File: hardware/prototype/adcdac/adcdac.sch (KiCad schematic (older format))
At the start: 68 parts, among them IC1 ADP3335, IC2 AD8138, IC3 AD8138, IC4 ADP3335, IC5 AD9744, IC6 ADP3335, IC7 ADP3335, IC8 AD8041, IC9 AD9218, J1 FPGA_GPIO0, J2 MODE, J3 S2, J4 S1, J5 DFS, P1 COAX, P2 COAX, P3 COAX

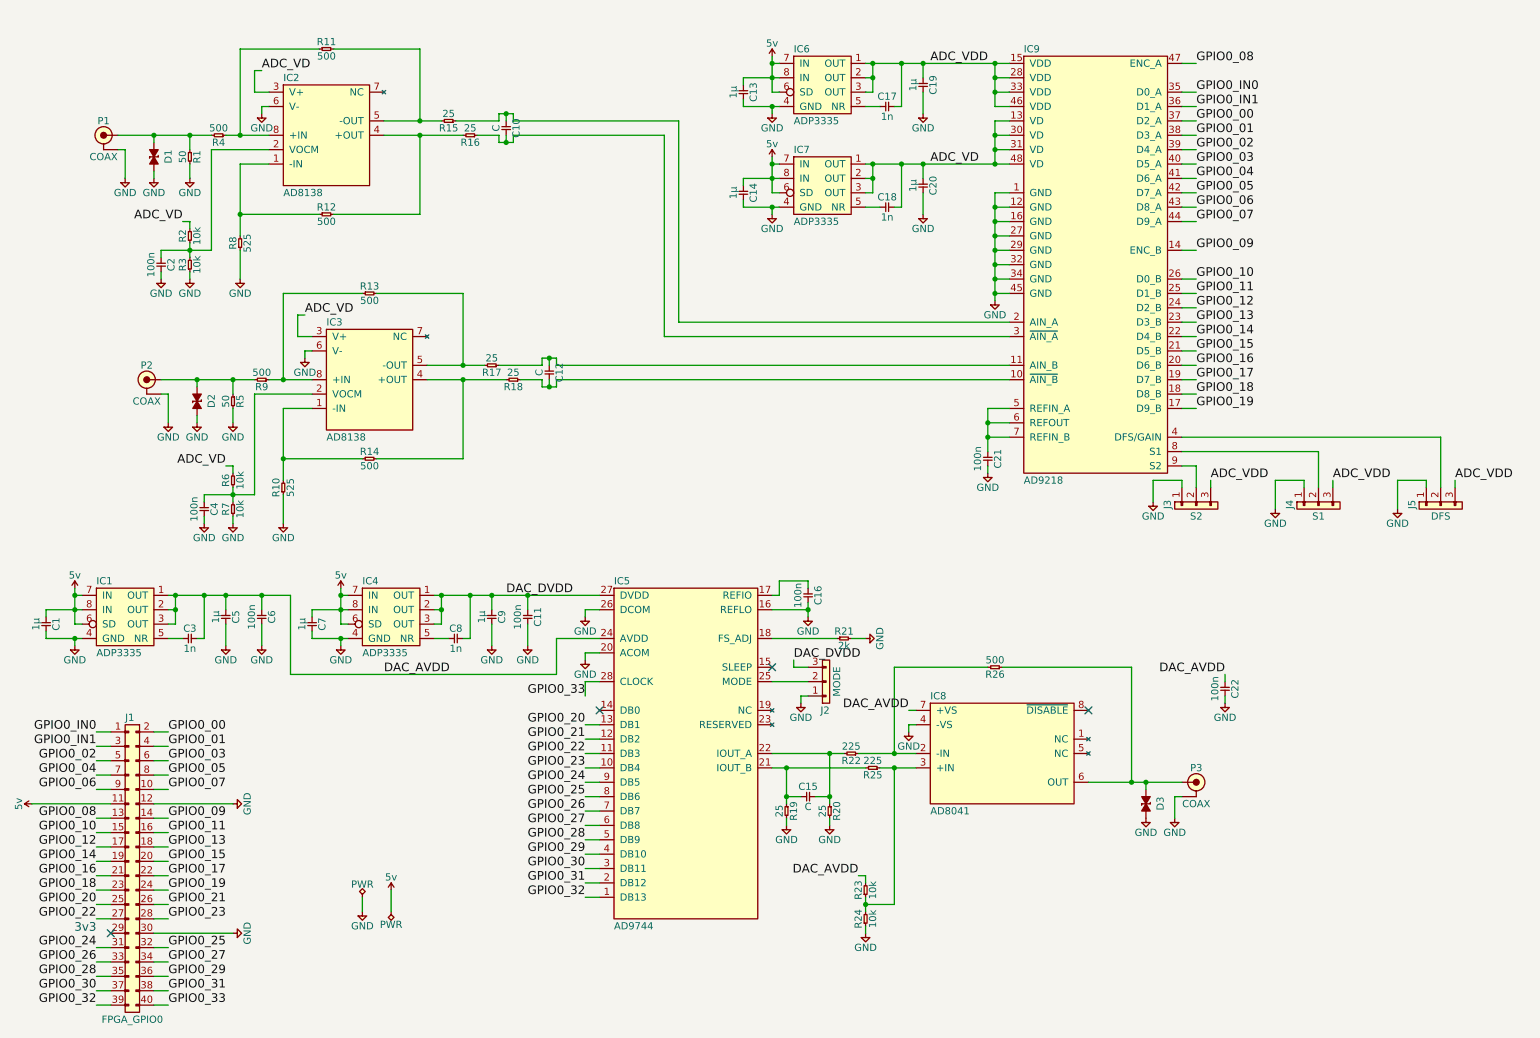
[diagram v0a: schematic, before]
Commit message: Minor sch tweaks
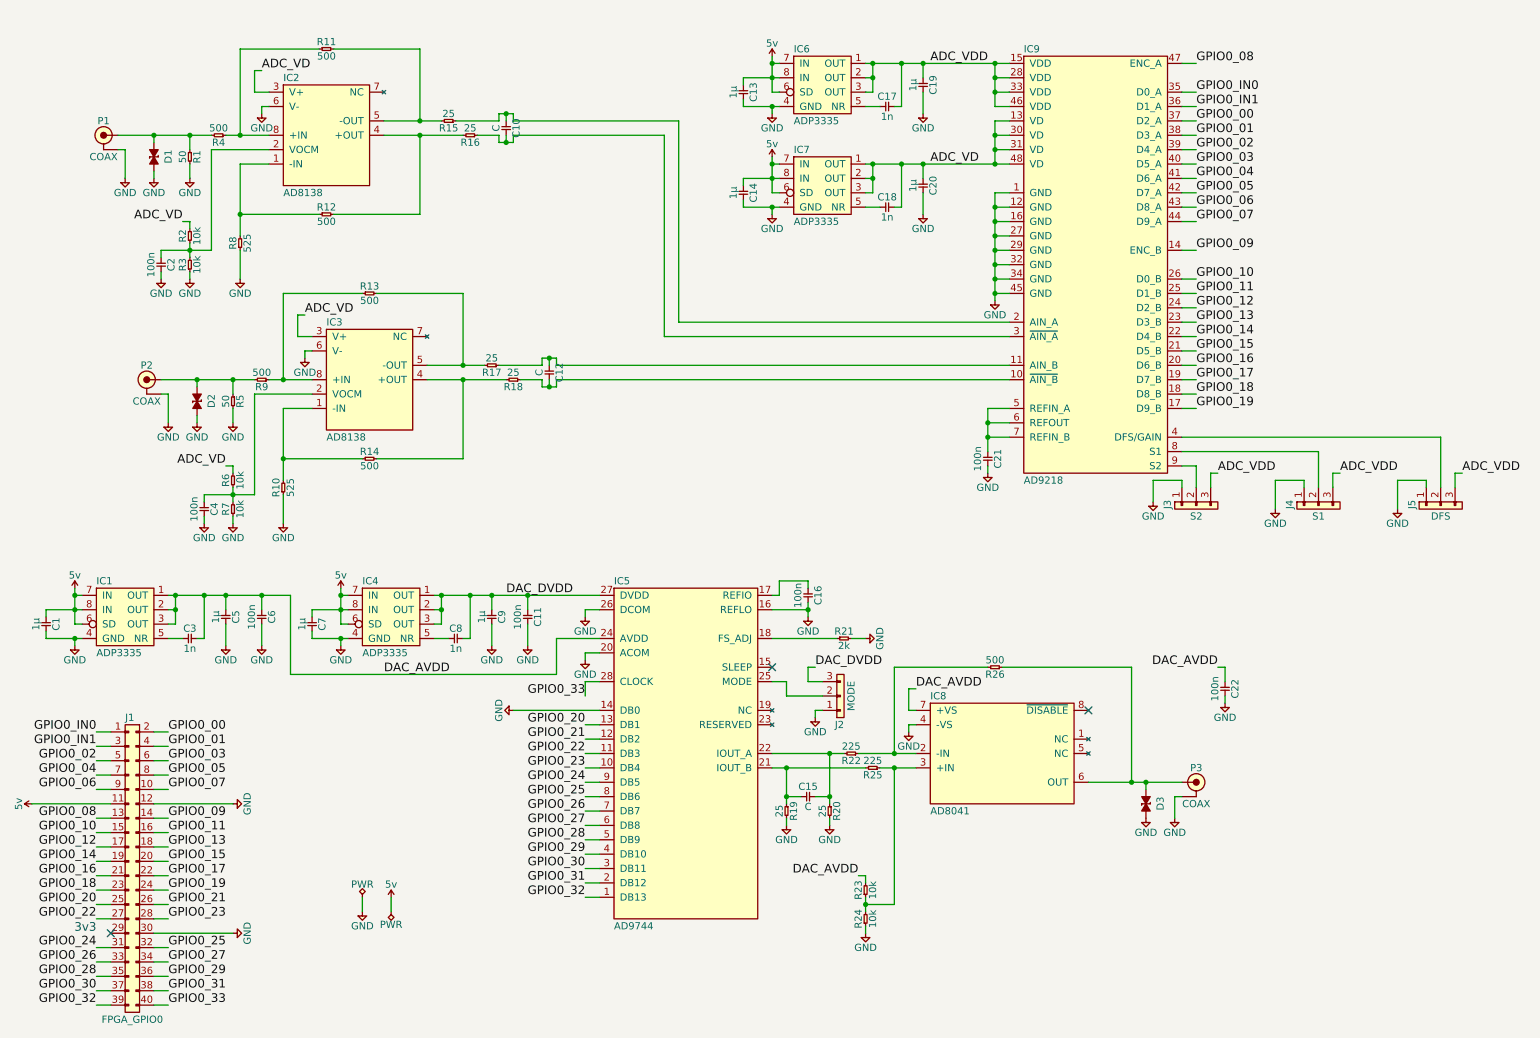
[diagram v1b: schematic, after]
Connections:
- net GND: now also IC5.14 (DB0)
- no-connect marks 4 -> 3
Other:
- moved on the sheet: J2
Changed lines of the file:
@@
 Text Label 8900 3350 0    60   ~ 0
 GPIO0_19
-NoConn ~ 4750 5450
 $Comp
 L 5v #PWR021
@@
 $EndComp
 NoConn ~ 8150 5450
-Text Label 6900 5450 2    60   ~ 0
+Text Label 6950 5300 0    60   ~ 0
 DAC_AVDD
 $Comp
@@
 Text Label 7050 1650 0    60   ~ 0
 ADC_VD
-Text Label 9100 5200 2    60   ~ 0
+Text Label 9050 5150 2    60   ~ 0
 DAC_AVDD
 $Comp
@@
 L CONN_01x03 J2
 U 1 1 59FA3731
-P 6300 5350
-F 0 "J2" H 6250 5450 50  0000 L CNN
-F 1 "MODE" V 6200 5250 50  0000 C CNN
-F 2 "agg:SIL-254P-03" H 6300 5350 50  0001 C CNN
-F 3 "" H 6300 5350 50  0001 C CNN
-	1    6300 5350
+P 6400 5450
+F 0 "J2" H 6350 5550 50  0000 L CNN
+F 1 "MODE" V 6300 5350 50  0000 C CNN
+F 2 "agg:SIL-254P-03" H 6400 5450 50  0001 C CNN
+F 3 "" H 6400 5450 50  0001 C CNN
+	1    6400 5450
 	-1   0    0    1
 $EndComp
@@
 L GND #PWR032
 U 1 1 59FA3B32
-P 6150 5400
-F 0 "#PWR032" H 6020 5440 50  0001 L CNN
-F 1 "GND" H 6150 5300 50  0000 C CNN
-F 2 "" H 6150 5400 60  0001 C CNN
-F 3 "" H 6150 5400 60  0001 C CNN
-	1    6150 5400
+P 6250 5500
+F 0 "#PWR032" H 6120 5540 50  0001 L CNN
+F 1 "GND" H 6250 5400 50  0000 C CNN
+F 2 "" H 6250 5500 60  0001 C CNN
+F 3 "" H 6250 5500 60  0001 C CNN
+	1    6250 5500
 	1    0    0    -1
 $EndComp
 Text Label 4100 4650 0    60   ~ 0
 DAC_DVDD
-Text Label 6100 5100 0    60   ~ 0
+Text Label 6250 5150 0    60   ~ 0
 DAC_DVDD
 $Comp
@@
 Text Label 7050 950  0    60   ~ 0
 ADC_VDD
-Text Label 9000 3850 0    60   ~ 0
+Text Label 9050 3800 0    60   ~ 0
 ADC_VDD
-Text Label 9850 3850 0    60   ~ 0
+Text Label 9900 3800 0    60   ~ 0
 ADC_VDD
-Text Label 10700 3850 0    60   ~ 0
+Text Label 10750 3800 0    60   ~ 0
 ADC_VDD
 $Comp
@@
 	9100 5400 9100 5350
 Wire Wire Line
-	9100 5200 9100 5250
+	9100 5150 9100 5250
 Wire Wire Line
 	5950 4750 6200 4750
@@
 	6400 4950 5950 4950
 Wire Wire Line
-	6200 5250 5950 5250
-Wire Wire Line
-	6200 5350 6150 5350
-Wire Wire Line
-	6150 5350 6150 5400
-Wire Wire Line
-	6100 5100 6100 5150
-Wire Wire Line
-	6100 5150 6200 5150
+	6300 5350 6050 5350
+Wire Wire Line
+	6300 5450 6250 5450
+Wire Wire Line
+	6250 5450 6250 5500
+Wire Wire Line
+	6200 5150 6200 5250
+Wire Wire Line
+	6200 5250 6300 5250
 Wire Wire Line
 	8800 3750 8900 3750
@@
 	10600 3550 10600 3900
 Wire Wire Line
-	9000 3850 9000 3900
-Wire Wire Line
-	9850 3850 9850 3900
-Wire Wire Line
-	10700 3850 10700 3900
+	9000 3800 9000 3900
+Wire Wire Line
+	9850 3800 9850 3900
+Wire Wire Line
+	10700 3800 10700 3900
 Wire Wire Line
 	8600 4000 8600 3850
@@
 L 5v #PWR048
 U 1 1 59FB00DD
-P 3300 6700
-F 0 "#PWR048" H 3300 6810 50  0001 L CNN
-F 1 "5v" H 3300 6790 50  0000 C CNN
-F 2 "" H 3300 6700 60  0001 C CNN
-F 3 "" H 3300 6700 60  0001 C CNN
-	1    3300 6700
+P 3300 6750
+F 0 "#PWR048" H 3300 6860 50  0001 L CNN
+F 1 "5v" H 3300 6840 50  0000 C CNN
+F 2 "" H 3300 6750 60  0001 C CNN
+F 3 "" H 3300 6750 60  0001 C CNN
+	1    3300 6750
 	1    0    0    -1
 $EndComp
@@
 $EndComp
 Wire Wire Line
-	3300 6850 3300 6700
+	3300 6850 3300 6750
 NoConn ~ 1350 7000
 Text Notes 1250 7000 2    60   ~ 0
@@
 Wire Wire Line
 	2700 2950 2750 2950
+$Comp
+L GND #PWR?
+U 1 1 59FB4DA3
+P 4150 5450
+F 0 "#PWR?" H 4020 5490 50  0001 L CNN
+F 1 "GND" H 4150 5350 50  0000 C CNN
+F 2 "" H 4150 5450 60  0001 C CNN
+F 3 "" H 4150 5450 60  0001 C CNN
+	1    4150 5450
+	0    1    1    0
+$EndComp
+Wire Wire Line
+	4150 5450 4750 5450
+Wire Wire Line
+	6950 5300 6900 5300
+Wire Wire Line
+	6900 5300 6900 5450
+Wire Wire Line
+	6250 5150 6200 5150
+Wire Wire Line
+	5950 5250 6050 5250
+Wire Wire Line
+	6050 5250 6050 5350
+Wire Wire Line
+	9050 3800 9000 3800
+Wire Wire Line
+	9900 3800 9850 3800
+Wire Wire Line
+	10750 3800 10700 3800
+Wire Wire Line
+	9050 5150 9100 5150
 $EndSCHEMATC

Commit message: finish routing, order r1 boards
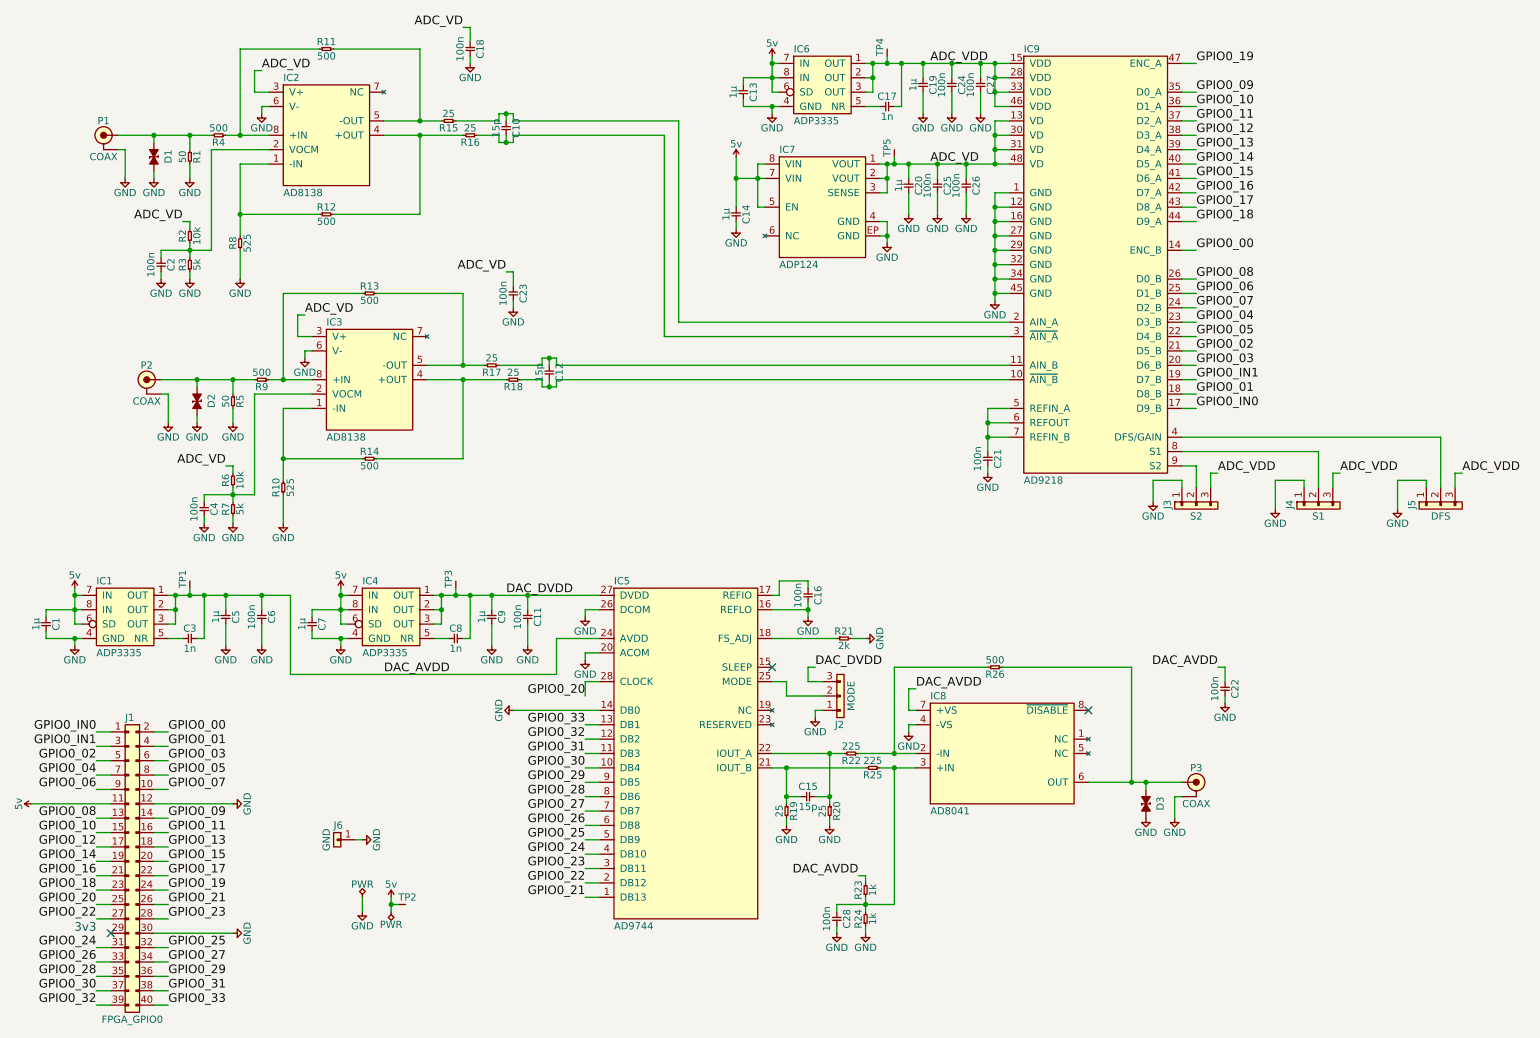
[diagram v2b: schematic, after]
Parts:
- removed IC7: ADP3335, agg:MSOP-8, symbol ADP3335
- added C23, C24, C25, C26, C27, C28: 100n, agg:0603, symbol C
- added IC7: ADP124, agg:MSOP-8-EP-AD, symbol ADP124
- added J6: GND, agg:SIL-254P-01, symbol CONN_01x01
- added TP1, TP2, TP3, TP4, TP5: TESTPAD, agg:TESTPAD, symbol TESTPAD
- C10, C12, C15: value C -> 15p
- C18: value 1n -> 100n
- J1: Farnell (none) -> 1885912
- P1, P2, P3: footprint (none) -> agg:BNC_PCB_RA_5-1634556-0; Farnell (none) -> 1248952
- R23, R24: value 10k -> 1k
- R3, R7: value 10k -> 5k
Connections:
- net 5v: now also IC7.5 (EN), IC7.7 (VIN), IC7.8 (VIN), TP2.1 (TP)
- net ADC_VD: now also C18.1, C23.1, C25.1, C26.1, IC7.1 (VOUT), IC7.2 (VOUT), IC7.3 (SENSE), TP5.1 (TP); no longer C18.2
- net ADC_VDD: now also C24.1, C27.1, TP4.1 (TP)
- net DAC_AVDD: now also TP1.1 (TP)
- net DAC_DVDD: now also TP3.1 (TP)
- net GND: now also C18.2, C23.2, C24.2, C25.2, C26.2, C27.2, C28.2, IC7.4 (GND), IC7.EP (GND), J6.1
- net GPIO0_00: now also IC9.14 (ENC_B); no longer IC9.37 (D2_A)
- net GPIO0_01: now also IC9.18 (D8_B); no longer IC9.38 (D3_A)
- net GPIO0_02: now also IC9.21 (D5_B); no longer IC9.39 (D4_A)
- net GPIO0_03: now also IC9.20 (D6_B); no longer IC9.40 (D5_A)
- net GPIO0_04: now also IC9.23 (D3_B); no longer IC9.41 (D6_A)
- net GPIO0_05: now also IC9.22 (D4_B); no longer IC9.42 (D7_A)
- net GPIO0_06: now also IC9.25 (D1_B); no longer IC9.43 (D8_A)
- net GPIO0_07: now also IC9.24 (D2_B); no longer IC9.44 (D9_A)
- net GPIO0_08: now also IC9.26 (D0_B); no longer IC9.47 (ENC_A)
- net GPIO0_09: now also IC9.35 (D0_A); no longer IC9.14 (ENC_B)
- net GPIO0_10: now also IC9.36 (D1_A); no longer IC9.26 (D0_B)
- net GPIO0_11: now also IC9.37 (D2_A); no longer IC9.25 (D1_B)
- net GPIO0_12: now also IC9.38 (D3_A); no longer IC9.24 (D2_B)
- net GPIO0_13: now also IC9.39 (D4_A); no longer IC9.23 (D3_B)
- net GPIO0_14: now also IC9.40 (D5_A); no longer IC9.22 (D4_B)
- net GPIO0_15: now also IC9.41 (D6_A); no longer IC9.21 (D5_B)
- net GPIO0_16: now also IC9.42 (D7_A); no longer IC9.20 (D6_B)
- net GPIO0_17: now also IC9.43 (D8_A); no longer IC9.19 (D7_B)
- net GPIO0_18: now also IC9.44 (D9_A); no longer IC9.18 (D8_B)
- net GPIO0_19: now also IC9.47 (ENC_A); no longer IC9.17 (D9_B)
- net GPIO0_20: now also IC5.28 (CLOCK); no longer IC5.13 (DB1)
- net GPIO0_21: now also IC5.1 (DB13); no longer IC5.12 (DB2)
- net GPIO0_22: now also IC5.2 (DB12); no longer IC5.11 (DB3)
- net GPIO0_23: now also IC5.3 (DB11); no longer IC5.10 (DB4)
- net GPIO0_24: now also IC5.4 (DB10); no longer IC5.9 (DB5)
- net GPIO0_25: now also IC5.5 (DB9); no longer IC5.8 (DB6)
- net GPIO0_26: now also IC5.6 (DB8); no longer IC5.7 (DB7)
- net GPIO0_27: now also IC5.7 (DB7); no longer IC5.6 (DB8)
- net GPIO0_28: now also IC5.8 (DB6); no longer IC5.5 (DB9)
- net GPIO0_29: now also IC5.9 (DB5); no longer IC5.4 (DB10)
- net GPIO0_30: now also IC5.10 (DB4); no longer IC5.3 (DB11)
- net GPIO0_31: now also IC5.11 (DB3); no longer IC5.2 (DB12)
- net GPIO0_32: now also IC5.12 (DB2); no longer IC5.1 (DB13)
- net GPIO0_33: now also IC5.13 (DB1); no longer IC5.28 (CLOCK)
- net GPIO0_IN0: now also IC9.17 (D9_B); no longer IC9.35 (D0_A)
- net GPIO0_IN1: now also IC9.19 (D7_B); no longer IC9.36 (D1_A)
- net at IC8.3 (+IN), R23.1, R24.2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: now also C28.1
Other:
- moved on the sheet: C14, C20

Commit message: assign part numbers, generate bom
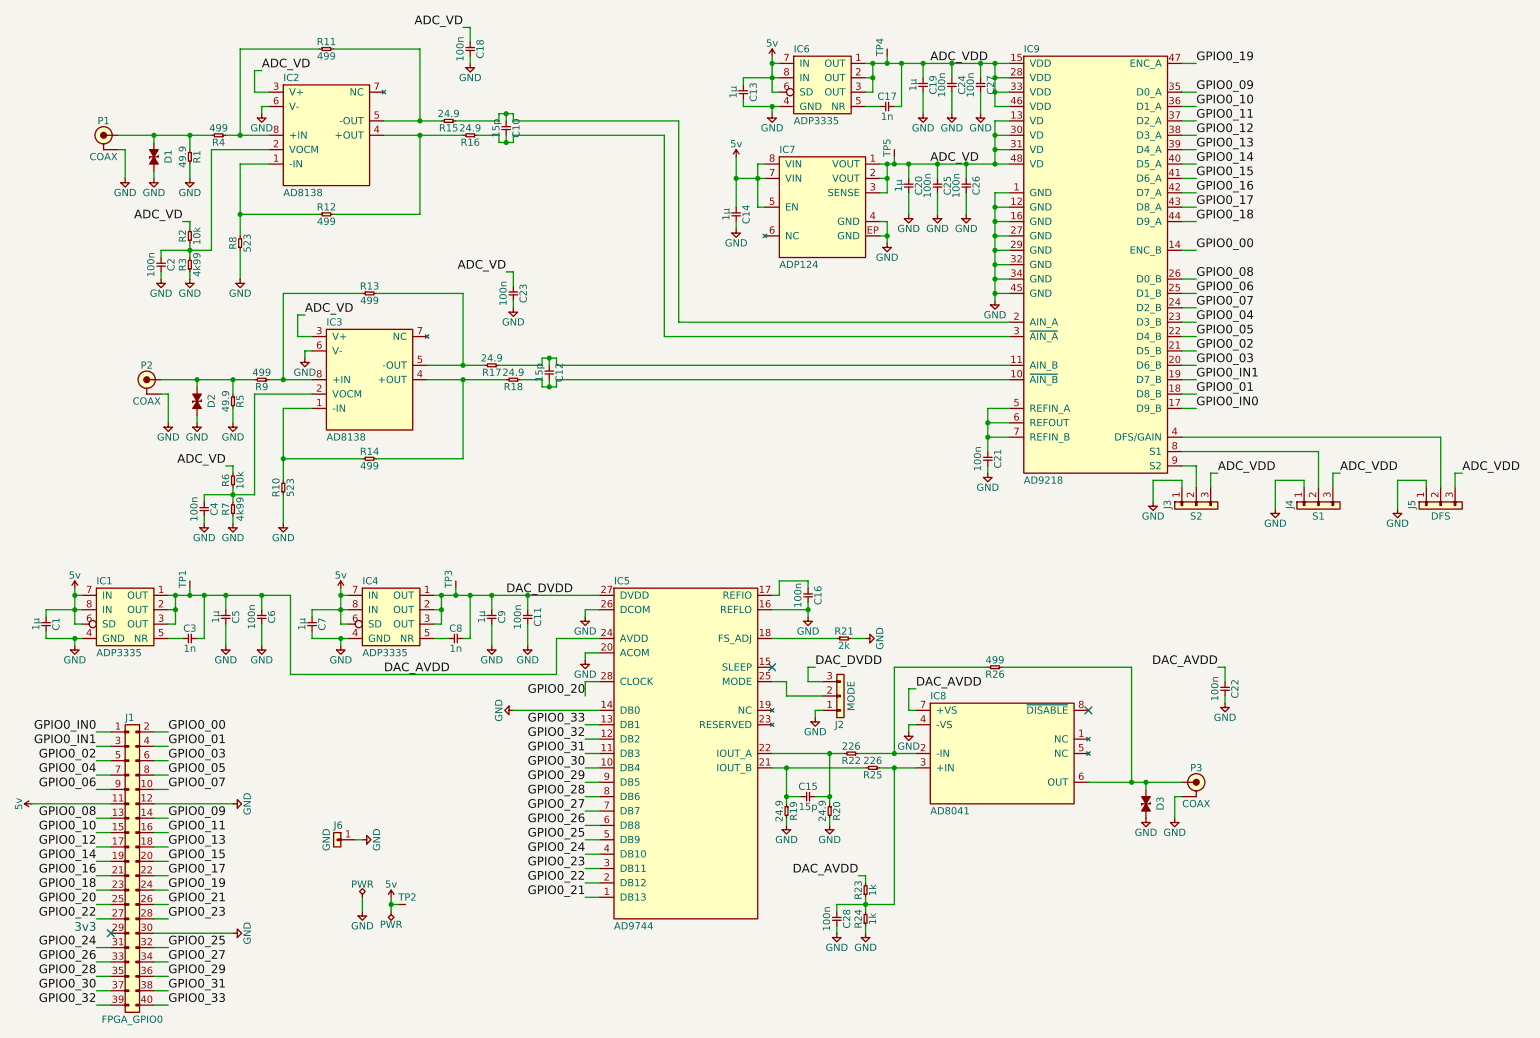
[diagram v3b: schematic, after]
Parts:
- C1, C13, C14, C19, C20, C5, C7, C9: Farnell (none) -> 2320814
- C10, C12, C15: Farnell (none) -> 721980
- C11, C16, C18, C2, C21, C22, C23, C24, C25, C26, C27, C28, C4, C6: Farnell (none) -> 1759122
- C17, C3, C8: Farnell (none) -> 1759088
- J2, J3, J4, J5: Farnell (none) -> 3418297
- J6: Farnell (none) -> 2308549
- R1, R5: value 50 -> 49.9; Farnell (none) -> 2447381
- R10, R8: value 525 -> 523; Farnell (none) -> 2694888
- R11, R12, R13, R14, R26, R4, R9: value 500 -> 499; Farnell (none) -> 2694886
- R15, R16, R17, R18, R19, R20: value 25 -> 24.9; Farnell (none) -> 2447311
- R2, R6: Farnell (none) -> 2447230
- R21: Farnell (none) -> 2447319
- R22, R25: value 225 -> 226; Farnell (none) -> 2303091
- R23, R24: Farnell (none) -> 2447272
- R3, R7: value 5k -> 4k99; Farnell (none) -> 2337208

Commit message: update prototype adcdac board sch to new kicad version
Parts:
- C1, C10, C11, C12, C13, C14, C15, C16, C17, C18, C19, C2, C20, C21, C22, C23, C24, C25, C26, C27, C28, C3, C4, C5, C6, C7, C8, C9: symbol C -> agg-kicad:C
- D1, D2, D3: symbol ESD_DIODE -> agg-kicad:ESD_DIODE
- IC1, IC4, IC6: symbol ADP3335 -> agg-kicad:ADP3335
- IC2, IC3: symbol AD8138 -> agg-kicad:AD8138
- IC5: symbol AD9744 -> agg-kicad:AD9744
- IC7: symbol ADP124 -> agg-kicad:ADP124
- IC8: symbol AD8041 -> agg-kicad:AD8041
- IC9: symbol AD9218 -> agg-kicad:AD9218
- J1: symbol CONN_02x20 -> agg-kicad:CONN_02x20
- J2, J3, J4, J5: symbol CONN_01x03 -> agg-kicad:CONN_01x03
- J6: symbol CONN_01x01 -> agg-kicad:CONN_01x01
- P1, P2, P3: symbol COAX -> agg-kicad:COAX
- R1, R10, R11, R12, R13, R14, R15, R16, R17, R18, R19, R2, R20, R21, R22, R23, R24, R25, R26, R3, R4, R5, R6, R7, R8, R9: symbol R -> agg-kicad:R
- TP1, TP2, TP3, TP4, TP5: symbol TESTPAD -> agg-kicad:TESTPAD
